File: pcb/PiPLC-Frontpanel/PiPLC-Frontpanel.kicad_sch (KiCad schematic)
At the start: 21 parts, among them J1 Conn_02x12_Odd_Even, J2 KNX, J3 Wago Pin Header 1mm, J4 Wago Pin Header 1mm

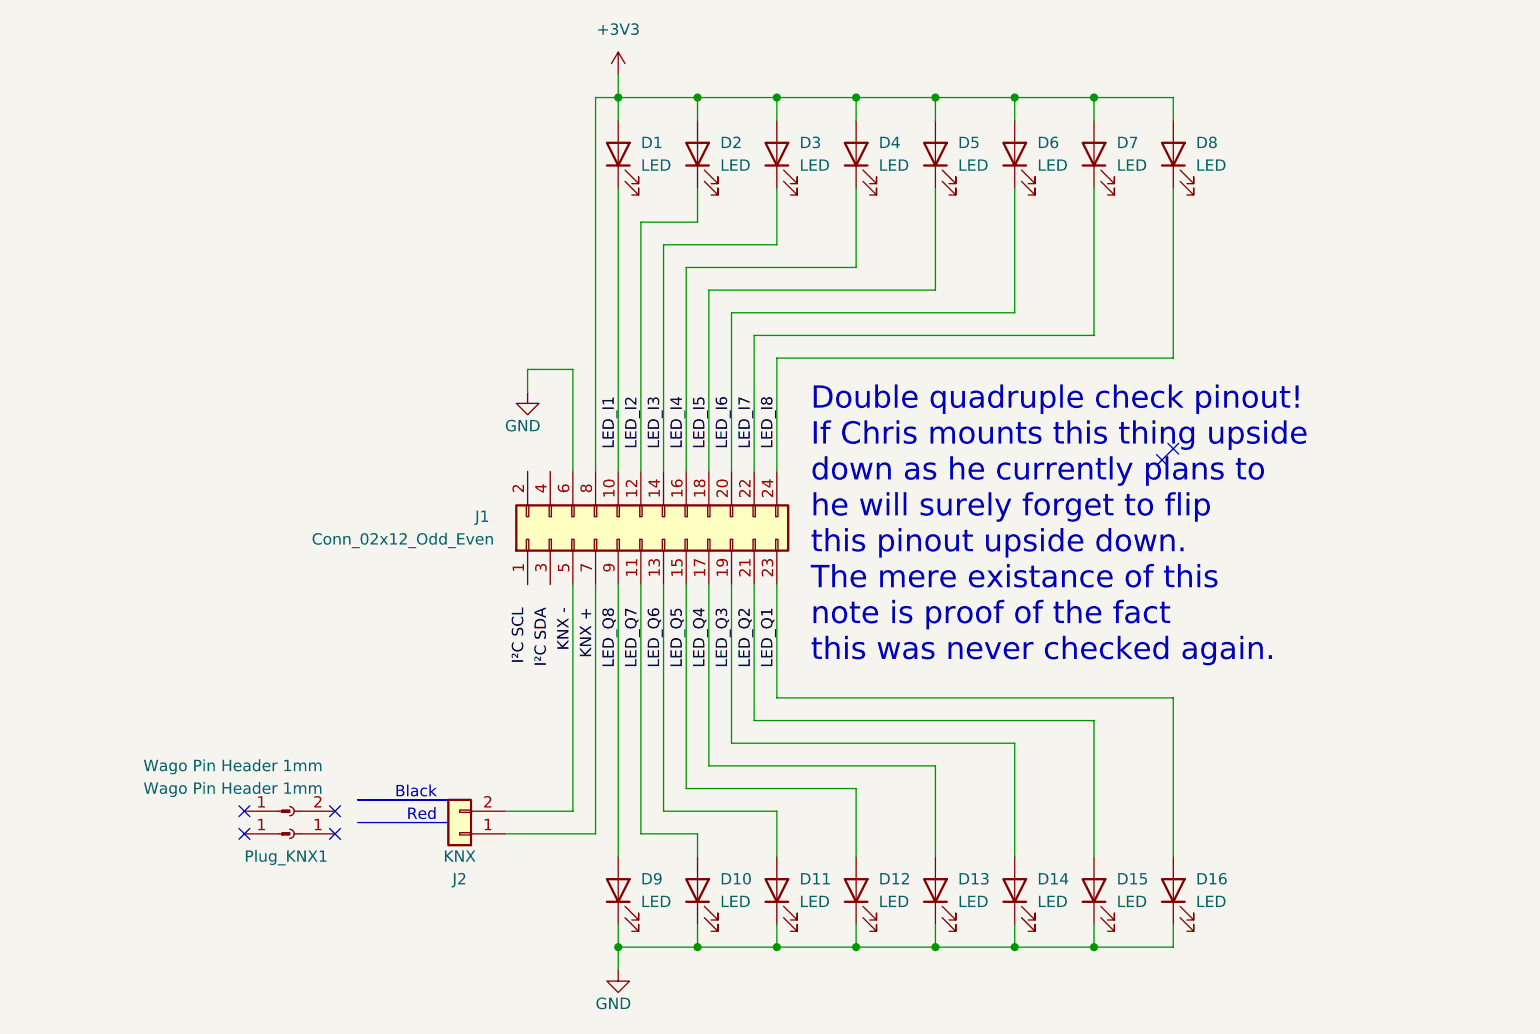
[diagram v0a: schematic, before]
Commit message: Throw all frontpanel pieces on the board somewhere
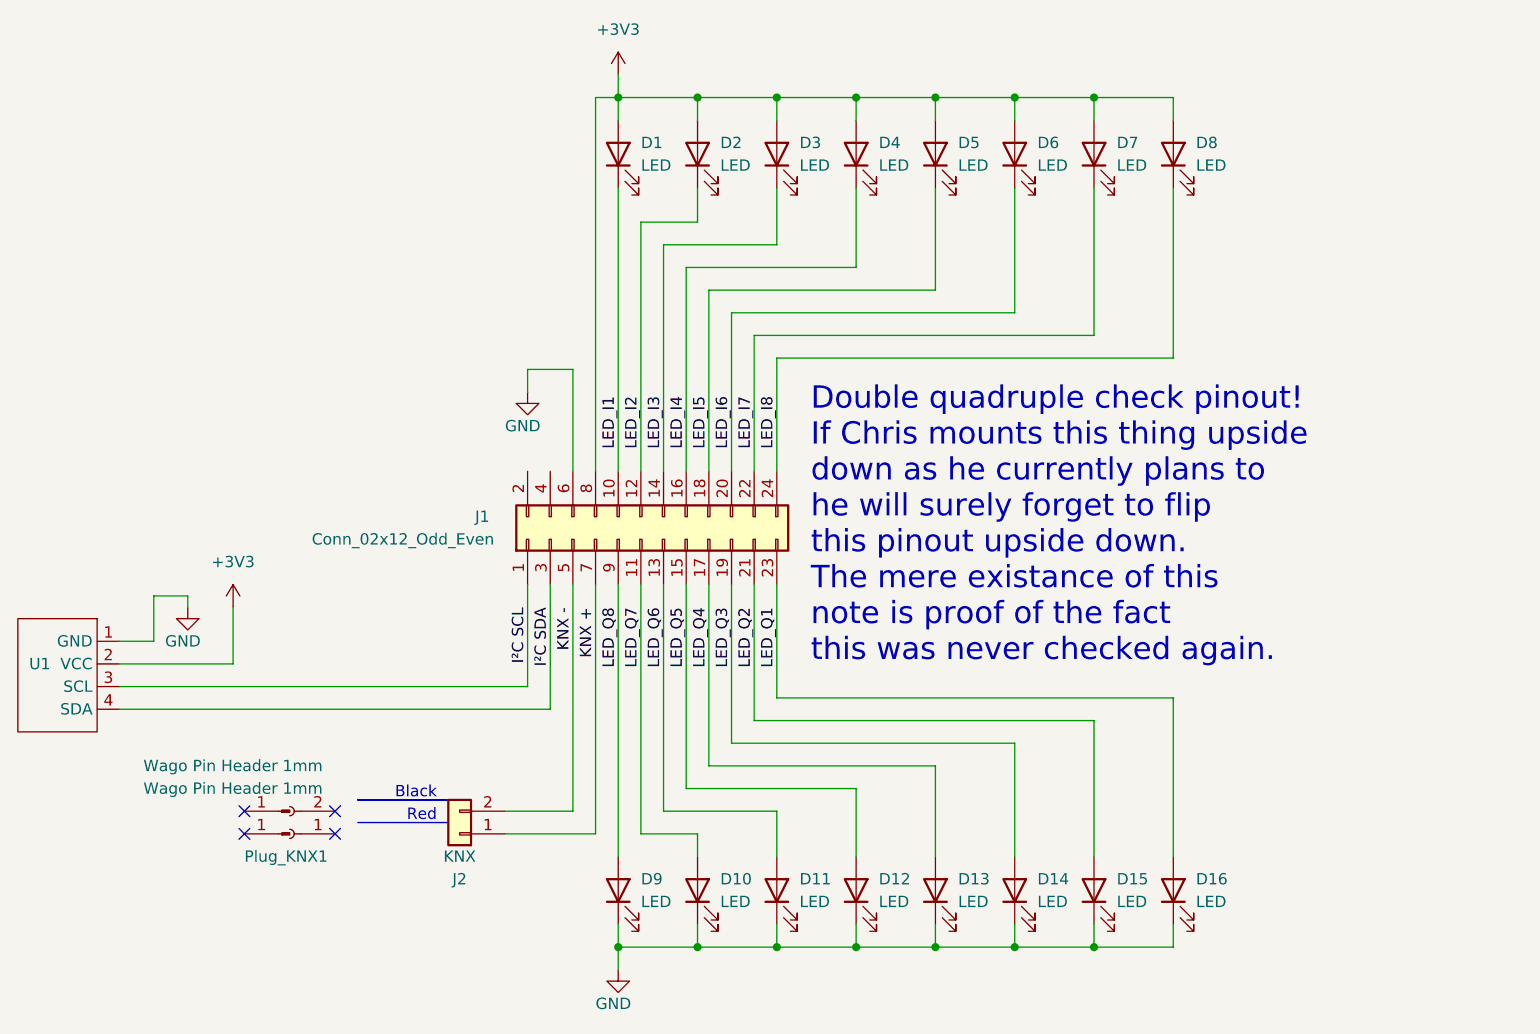
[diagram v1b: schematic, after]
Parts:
- added U1: ~, MeineBib:HS96L03, symbol MeineBib:HS96L03
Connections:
- net +3V3: now also U1.2 (VCC)
- net GND: now also U1.1 (GND)
- net I²C SCL: now also J1.1 (Pin_1), U1.3 (SCL)
- net I²C SDA: now also J1.3 (Pin_3), U1.4 (SDA)
- no-connect marks 6 -> 4
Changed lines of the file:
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@@
   (no_connect (at 118.11 123.19))
   (no_connect (at 118.11 125.73))
-  (no_connect (at 210.82 83.82))
-  (no_connect (at 212.09 82.55))
   (no_connect (at 107.95 123.19))
   (wire (pts (xy 176.53 120.65) (xy 157.48 120.65))
@@
     (stroke (width 0) (type solid))
   )
+  (wire (pts (xy 93.98 111.76) (xy 142.24 111.76))
+    (stroke (width 0) (type default))
+  )
   (wire (pts (xy 147.32 97.79) (xy 147.32 125.73))
     (stroke (width 0) (type default))
   )
+  (wire (pts (xy 106.68 106.68) (xy 93.98 106.68))
+    (stroke (width 0) (type default))
+  )
   (wire (pts (xy 147.32 125.73) (xy 137.16 125.73))
     (stroke (width 0) (type default))
@@
     (stroke (width 0) (type default))
   )
+  (wire (pts (xy 97.79 104.14) (xy 97.79 99.06))
+    (stroke (width 0) (type default))
+  )
   (wire (pts (xy 147.32 43.18) (xy 149.86 43.18))
     (stroke (width 0) (type default))
@@
     (stroke (width 0) (type default))
   )
+  (wire (pts (xy 101.6 99.06) (xy 101.6 100.33))
+    (stroke (width 0) (type default))
+  )
   (wire (pts (xy 176.53 62.23) (xy 176.53 53.34))
     (stroke (width 0) (type default))
@@
     (stroke (width 0) (type default))
   )
+  (wire (pts (xy 93.98 104.14) (xy 97.79 104.14))
+    (stroke (width 0) (type default))
+  )
   (wire (pts (xy 203.2 69.85) (xy 203.2 53.34))
     (stroke (width 0) (type default))
@@
     (stroke (width 0) (type default))
   )
+  (wire (pts (xy 139.7 97.79) (xy 139.7 109.22))
+    (stroke (width 0) (type default))
+  )
   (wire (pts (xy 158.75 128.27) (xy 158.75 125.73))
     (stroke (width 0) (type default))
@@
   )
   (wire (pts (xy 176.53 43.18) (xy 176.53 45.72))
+    (stroke (width 0) (type default))
+  )
+  (wire (pts (xy 142.24 97.79) (xy 142.24 111.76))
     (stroke (width 0) (type default))
   )
@@
     (stroke (width 0) (type default))
   )
+  (wire (pts (xy 106.68 100.33) (xy 106.68 106.68))
+    (stroke (width 0) (type default))
+  )
   (wire (pts (xy 152.4 125.73) (xy 152.4 97.79))
     (stroke (width 0) (type default))
@@
     (stroke (width 0) (type default))
   )
+  (wire (pts (xy 97.79 99.06) (xy 101.6 99.06))
+    (stroke (width 0) (type default))
+  )
   (wire (pts (xy 137.16 123.19) (xy 144.78 123.19))
     (stroke (width 0) (type default))
@@
   )
   (wire (pts (xy 176.53 138.43) (xy 167.64 138.43))
+    (stroke (width 0) (type default))
+  )
+  (wire (pts (xy 139.7 109.22) (xy 93.98 109.22))
     (stroke (width 0) (type default))
   )
@@
         (path "/8e79ca85-0324-46f6-b833-7804912a961b"
           (reference "D8") (unit 1)
+        )
+      )
+    )
+  )
+  (symbol (lib_id "MeineBib:HS96L03") (at 88.9 107.95 270) (unit 1)
+    (in_bom yes) (on_board yes) (dnp no)
+    (property "Reference" "U1" (at 83.82 106.68 90)
+      (effects (font (size 1.27 1.27)) (justify left))
+    )
+    (property "Value" "~" (at 88.9 107.95 0)
+      (effects (font (size 1.27 1.27)))
+    )
+    (property "Footprint" "MeineBib:HS96L03" (at 88.9 107.95 0)
+      (effects (font (size 1.27 1.27)) hide)
+    )
+    (property "Datasheet" "https://datasheet.lcsc.com/lcsc/2306271450_HS-HS96L03W2C03_C5248080.pdf" (at 88.9 107.95 0)
+      (effects (font (size 1.27 1.27)) hide)
+    )
+    (property "LCSC" "C5248080" (at 88.9 107.95 0)
+      (effects (font (size 1.27 1.27)) hide)
+    )
+    (pin "1")
+    (pin "2")
+    (pin "3")
+    (pin "4")
+    (instances
+      (project "PiPLC-Frontpanel"
+        (path "/8e79ca85-0324-46f6-b833-7804912a961b"
+          (reference "U1") (unit 1)
         )
       )
@@
         )
       )
+    )
+  )
+  (symbol (lib_id "power:GND") (at 101.6 100.33 0) (unit 1)
+    (in_bom yes) (on_board yes) (dnp no)
+    (property "Reference" "#PWR04" (at 101.6 106.68 0)
+      (effects (font (size 1.27 1.27)) hide)
+    )
+    (property "Value" "GND" (at 99.06 104.14 0)
+      (effects (font (size 1.27 1.27)) (justify left))
+    )
+    (property "Footprint" "" (at 101.6 100.33 0)
+      (effects (font (size 1.27 1.27)) hide)
+    )
+    (property "Datasheet" "" (at 101.6 100.33 0)
+      (effects (font (size 1.27 1.27)) hide)
+    )
+    (pin "1")
+    (instances
+      (project "PiPLC-Frontpanel"
+        (path "/8e79ca85-0324-46f6-b833-7804912a961b"
+          (reference "#PWR04") (unit 1)
+        )
+      )
+      (project "PiPLC-Base"
+        (path "/93ebf745-625a-4d9e-8f47-45e91f30ef94"
+          (reference "#PWR045") (unit 1)
+        )
+      )
+    )
+  )
+  (symbol (lib_id "power:+3V3") (at 106.68 100.33 0) (unit 1)
+    (in_bom yes) (on_board yes) (dnp no) (fields_autoplaced)
+    (property "Reference" "#PWR05" (at 106.68 104.14 0)
+      (effects (font (size 1.27 1.27)) hide)
+    )
+    (property "Value" "+3V3" (at 106.68 95.25 0)
+      (effects (font (size 1.27 1.27)))
+    )
+    (property "Footprint" "" (at 106.68 100.33 0)
+      (effects (font (size 1.27 1.27)) hide)
+    )
+    (property "Datasheet" "" (at 106.68 100.33 0)
+      (effects (font (size 1.27 1.27)) hide)
+    )
+    (pin "1")
+    (instances
+      (project "PiPLC-Frontpanel"
+        (path "/8e79ca85-0324-46f6-b833-7804912a961b"
+          (reference "#PWR05") (unit 1)
+        )
+      )
+      (project "PiPLC-Base"
+        (path "/93ebf745-625a-4d9e-8f47-45e91f30ef94"
+          (reference "#PWR046") (unit 1)
+        )
+      )
